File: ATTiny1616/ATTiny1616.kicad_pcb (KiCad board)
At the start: 2 copper layers, 18 x 35.1 mm, 30 parts, among them J1 Conn_01x10, J3 Conn_01x10, U1 AP2204K-ADJ, U2 ATtiny3216-M

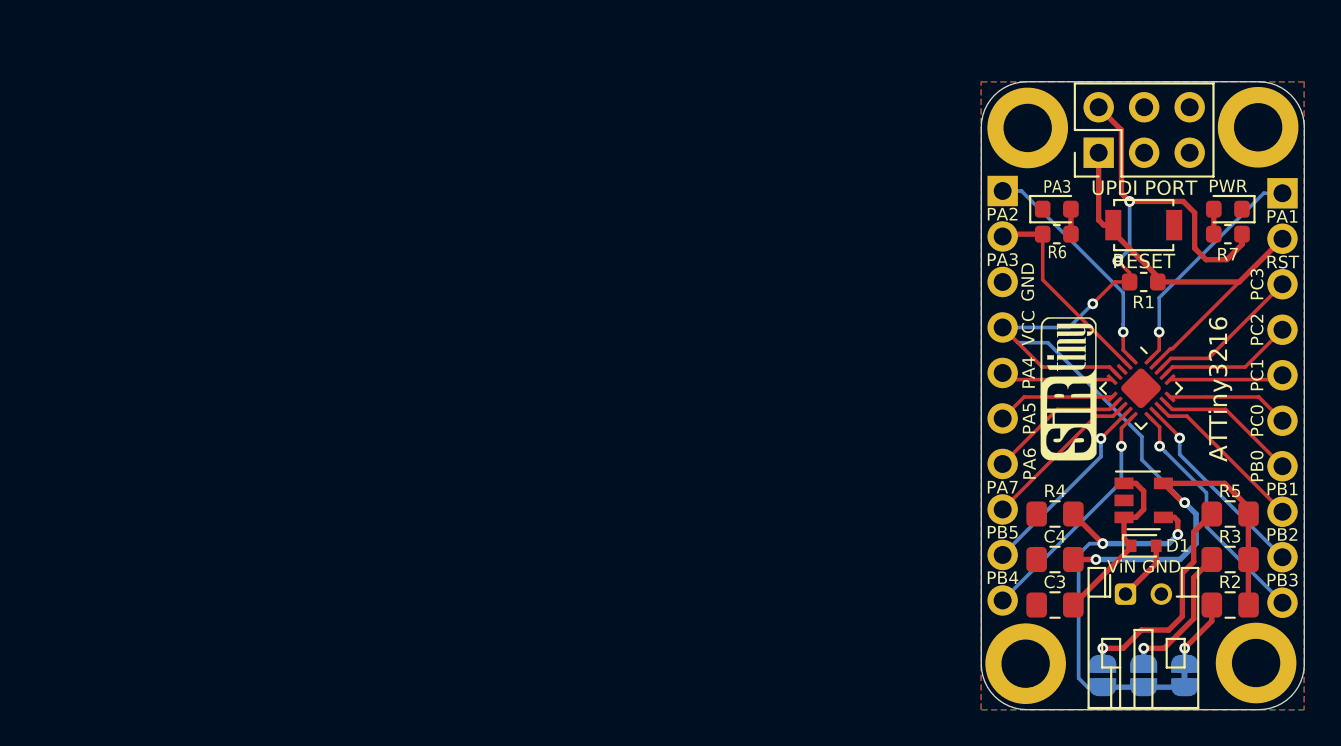
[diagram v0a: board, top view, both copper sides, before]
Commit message: Silkscreens Updated and Board Outlines aligned
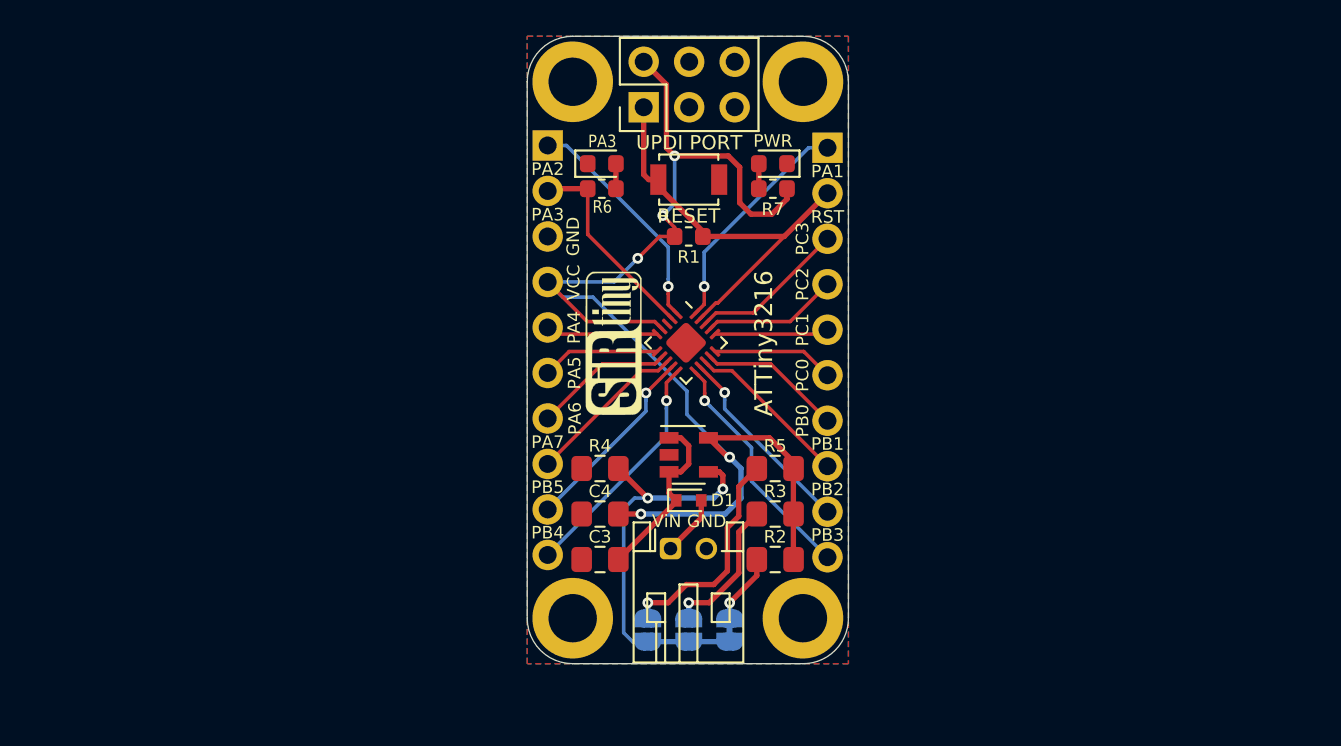
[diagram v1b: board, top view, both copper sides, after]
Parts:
- moved REF** 25.5 mm to (136.6, 74.8)
- moved C3 25.5 mm to (125.2, 101.5)
- moved C4 25.5 mm to (125.2, 98.9)
- moved R4 25.5 mm to (125.2, 96.4)
- moved REF** 25.5 mm to (123.7, 74.8)
- moved G*** 25.5 mm to (130.0, 83.4)
- moved J3 25.5 mm to (137.9, 78.5)
- moved PA3 25.5 mm to (125.3, 79.4)
- moved PWR 25.5 mm to (134.9, 79.4)
- moved R2 25.5 mm to (135.0, 101.5)
- moved R3 25.5 mm to (135.0, 98.9)
- moved R5 25.5 mm to (135.0, 96.4)
- moved R6 25.5 mm to (125.3, 80.8)
- moved R7 25.5 mm to (134.9, 80.8)
- moved REF** 25.5 mm to (123.6, 104.7)
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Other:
- board size 18 x 35.1 mm -> 17.9 x 35 mm

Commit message: Spacings Updated
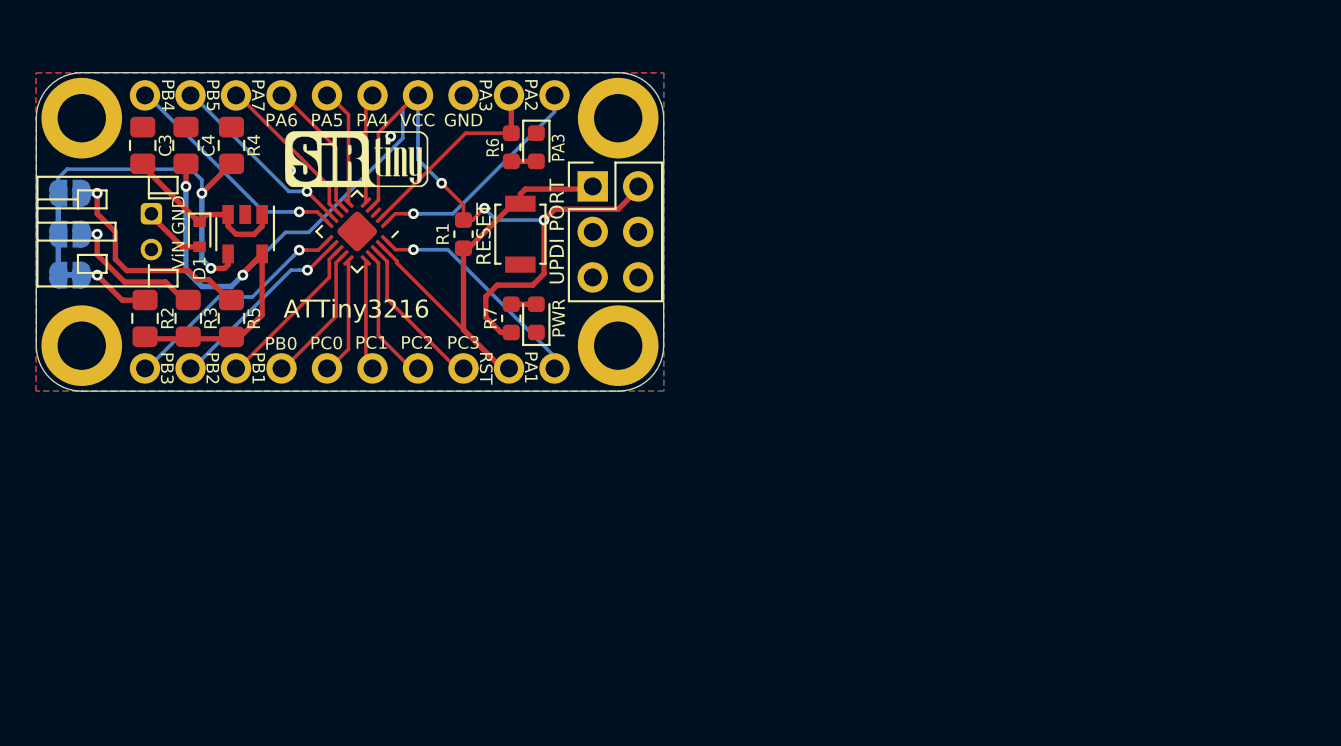
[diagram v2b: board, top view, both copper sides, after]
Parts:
- moved REF** 43.0 mm to (96.3, 89.5), turned to 270 degrees
- moved 5V 41.8 mm to (95.6, 85.6), turned to 180 degrees
- moved 3V3 41.0 mm to (95.6, 83.3), turned to 0 degrees
- moved 1V8 40.4 mm to (95.6, 81.0), turned to 0 degrees
- moved REF** 39.1 mm to (96.3, 76.7), turned to 270 degrees
- moved R2 37.7 mm to (99.8, 88.0), turned to 90 degrees
- moved R3 34.5 mm to (102.2, 88.0), turned to 90 degrees
- moved ViN GND 34.5 mm to (100.2, 82.2), turned to 270 degrees
- moved C3 34.4 mm to (99.7, 78.4), turned to 90 degrees
- moved R5 31.5 mm to (104.6, 88.0), turned to 90 degrees
- moved D1 31.1 mm to (102.9, 83.3), turned to 270 degrees
- moved C4 30.9 mm to (102.1, 78.4), turned to 90 degrees
- moved G*** 27.7 mm to (105.4, 83.3), turned to 90 degrees
- moved U1 27.7 mm to (105.4, 83.3), turned to 270 degrees
- moved R4 27.4 mm to (104.6, 78.4), turned to 90 degrees
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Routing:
- net GND: vias 0 -> 2
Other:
- board size 17.9 x 35 mm -> 35 x 17.8 mm

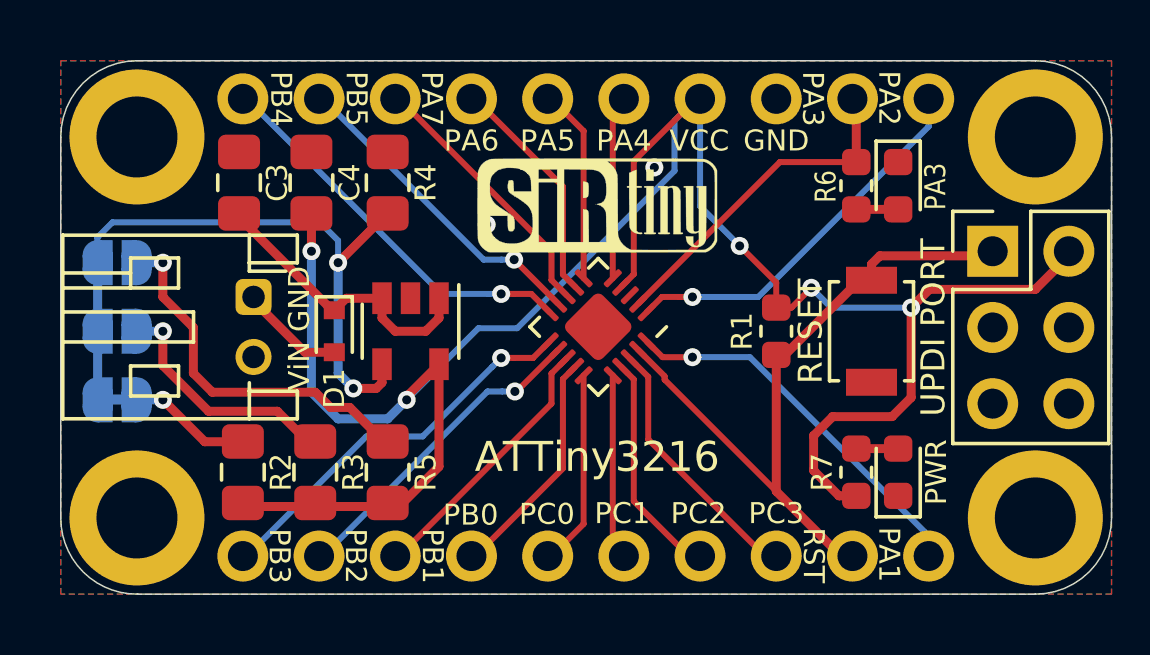
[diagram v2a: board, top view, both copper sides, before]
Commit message: Silkscreens Orientated
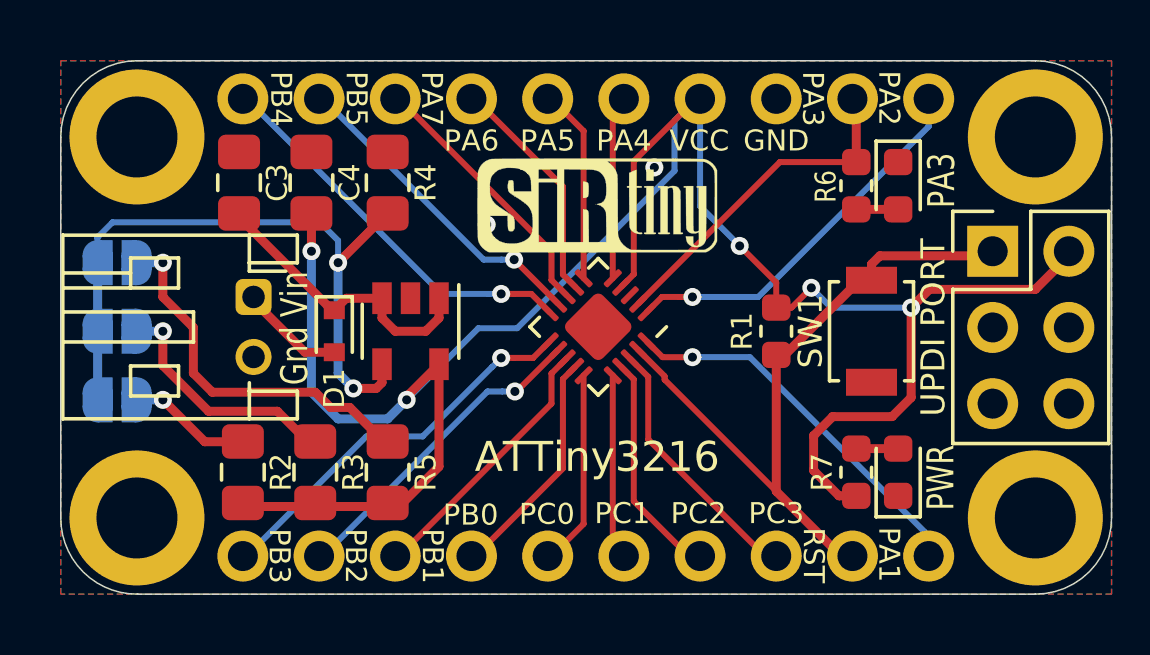
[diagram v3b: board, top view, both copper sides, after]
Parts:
- removed the 5V at (95.6, 85.6)
- added 5V: SolderJumper_2_Open, Jumper:SolderJumper-2_P1.3mm_Open_RoundedPad1.0x1.5mm, B.Cu at (95.6, 85.6)
- Gnd Vin: renamed from ViN GND
- renumbered RESET to SW1
